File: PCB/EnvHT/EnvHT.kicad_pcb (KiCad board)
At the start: 2 copper layers, 29.5 x 18.2 mm, 24 parts, among them J1 DC, J2 DC, J4 Shelly, U1 LMR16006XDDCR, U4 ESP32-PICO-MINI-02, U7 SHT40

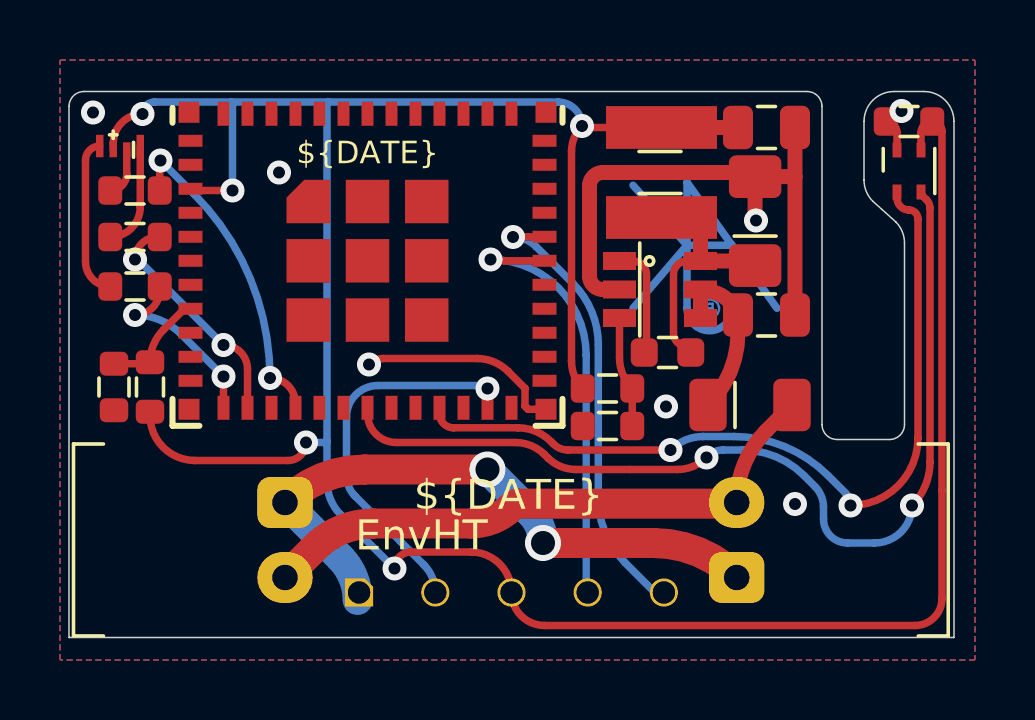
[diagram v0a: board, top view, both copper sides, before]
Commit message: Screw adjust
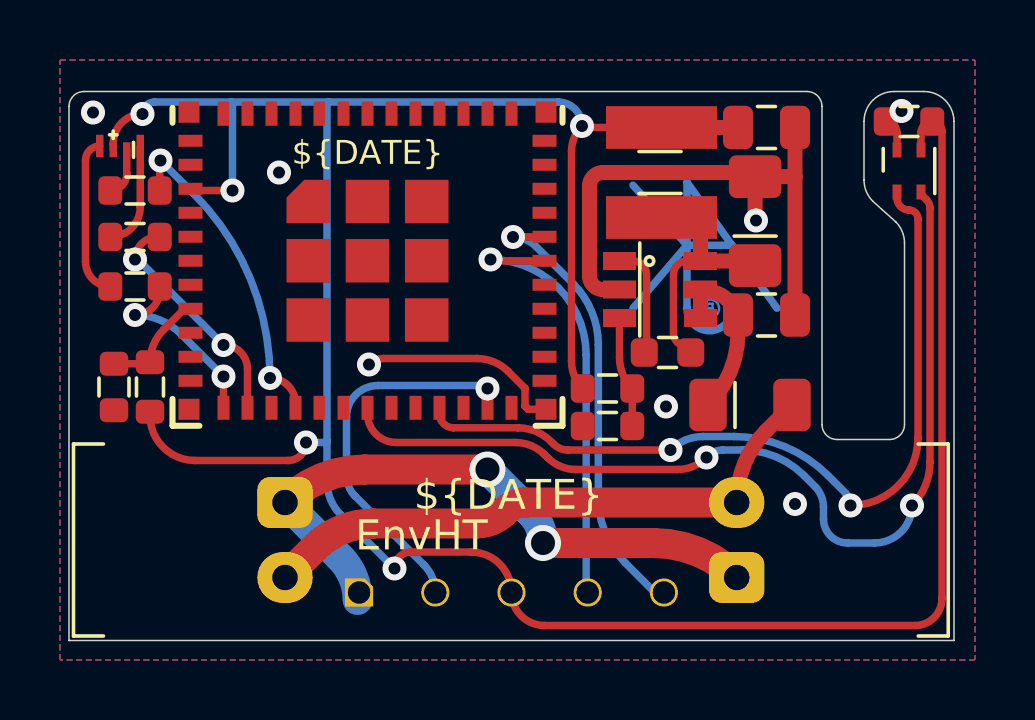
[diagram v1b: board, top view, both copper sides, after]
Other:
- board size 29.5 x 18.2 mm -> 29.5 x 18.3 mm

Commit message: Screws
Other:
- board text added: "SDA: 15 SCL: 14 RGB: 25/33/32"
- board text removed: "SDA: 15 SCL: 14"
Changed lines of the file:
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@@
 (kicad_pcb (version 20221018) (generator pcbnew)
   (general
-    (thickness 0.8)
+    (thickness 1.6)
   )
   (paper "A4")
@@
       (layer "F.Mask" (type "Top Solder Mask") (color "Purple") (thickness 0.01))
       (layer "F.Cu" (type "copper") (thickness 0.035))
-      (layer "dielectric 1" (type "core") (thickness 0.71) (material "FR4") (epsilon_r 4.5) (loss_tangent 0.02))
+      (layer "dielectric 1" (type "core") (thickness 1.51) (material "FR4") (epsilon_r 4.5) (loss_tangent 0.02))
       (layer "B.Cu" (type "copper") (thickness 0.035))
       (layer "B.Mask" (type "Bottom Solder Mask") (color "Purple") (thickness 0.01))
@@
       (stroke (width 0.1) (type solid)) (fill none) (layer "F.Fab"))
     (model "${REVK_3D}/M3.5CSK.step"
-      (offset (xyz 0 0 3))
+      (offset (xyz 0 0 6))
       (scale (xyz 1 1 1))
       (rotate (xyz 0 -90 0))
@@
       (stroke (width 0.1) (type solid)) (fill none) (layer "F.Fab"))
     (model "${REVK_3D}/M3.5CSK.step"
-      (offset (xyz 0 0 3))
+      (offset (xyz 0 0 6))
       (scale (xyz 1 1 1))
       (rotate (xyz 0 -90 0))
@@
         (effects (font (size 0.5 0.5) (thickness 0.08)) (justify mirror))
     )
-    (fp_text user "3.3" (at -0.7 0.7 315 unlocked) (layer "B.SilkS")
-        (effects (font (size 0.7 0.7) (thickness 0.1)) (justify mirror))
-    )
     (fp_text user "↓1" (at -5.91 0.8 315 unlocked) (layer "B.SilkS")
         (effects (font (size 0.5 0.5) (thickness 0.08)) (justify mirror))
@@
   (gr_line (start 88.3 78.8) (end 112.4 78.8)
     (stroke (width 0.05) (type solid)) (layer "Edge.Cuts"))
-  (gr_text "SDA: 15\nSCL: 14" (at 98 84) (layer "B.SilkS")
-    (effects (font (size 1 1) (thickness 0.15)) (justify mirror))
+  (gr_text "SDA: 15\nSCL: 14\nRGB: 25/33/32" (at 103.36 84.44) (layer "B.SilkS")
+    (effects (font (size 1 1) (thickness 0.15)) (justify left mirror))
   )
   (gr_text "⏚" (at 112.1 95 90) (layer "B.SilkS")
